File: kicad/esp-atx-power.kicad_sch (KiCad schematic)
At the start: 55 parts, among them J101 Conn_ARM_JTAG_SWD_10, J102 Conn_02x09_Odd_Even, J103 Conn_01x04, J105 GT-USB-7010ASV, K101 G3VM-61D1, K102 G3VM-61D1, K103 G3VM-61D1, K104 G3VM-61D1, SW101 TS-1187A-B-A-B, SW102 TS-1187A-B-A-B, U101 ESP32-C3-WROOM-02U, U102 AMS1117-3.3, U103 USBLC6-2P6, U104 TPS2116DRL

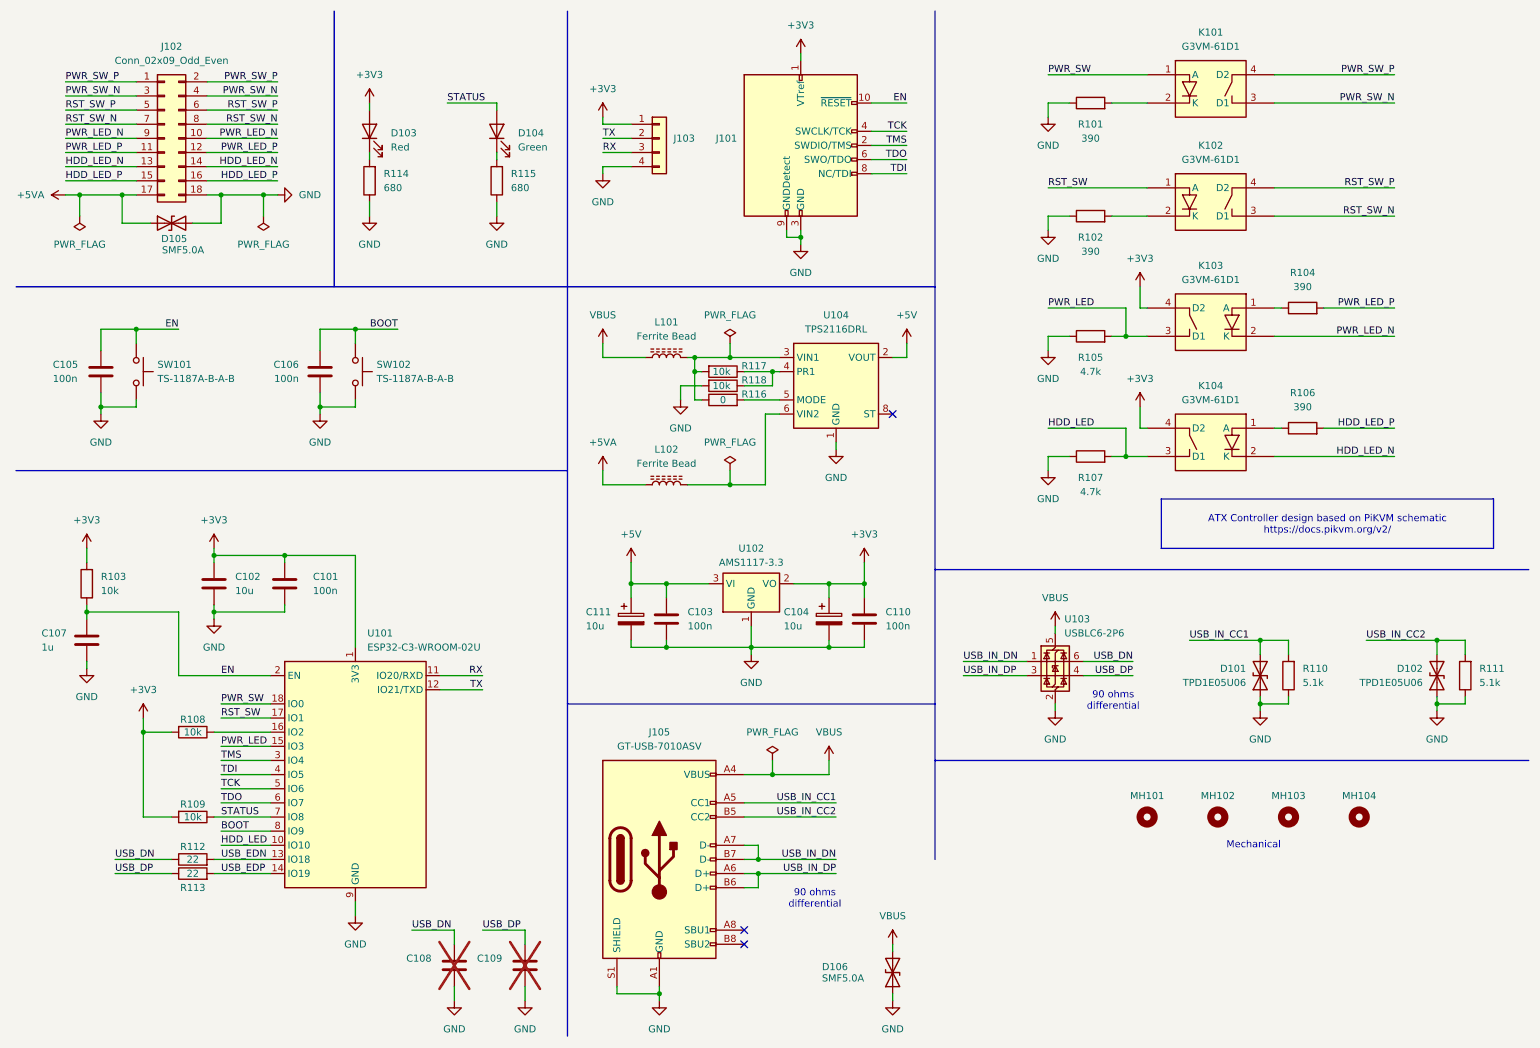
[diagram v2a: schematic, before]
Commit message: Fix TVS diode orientation
The selected diode was not bidirectional, update schematic symbol
to take it into account and fix orientation on VBUS (short circuit).
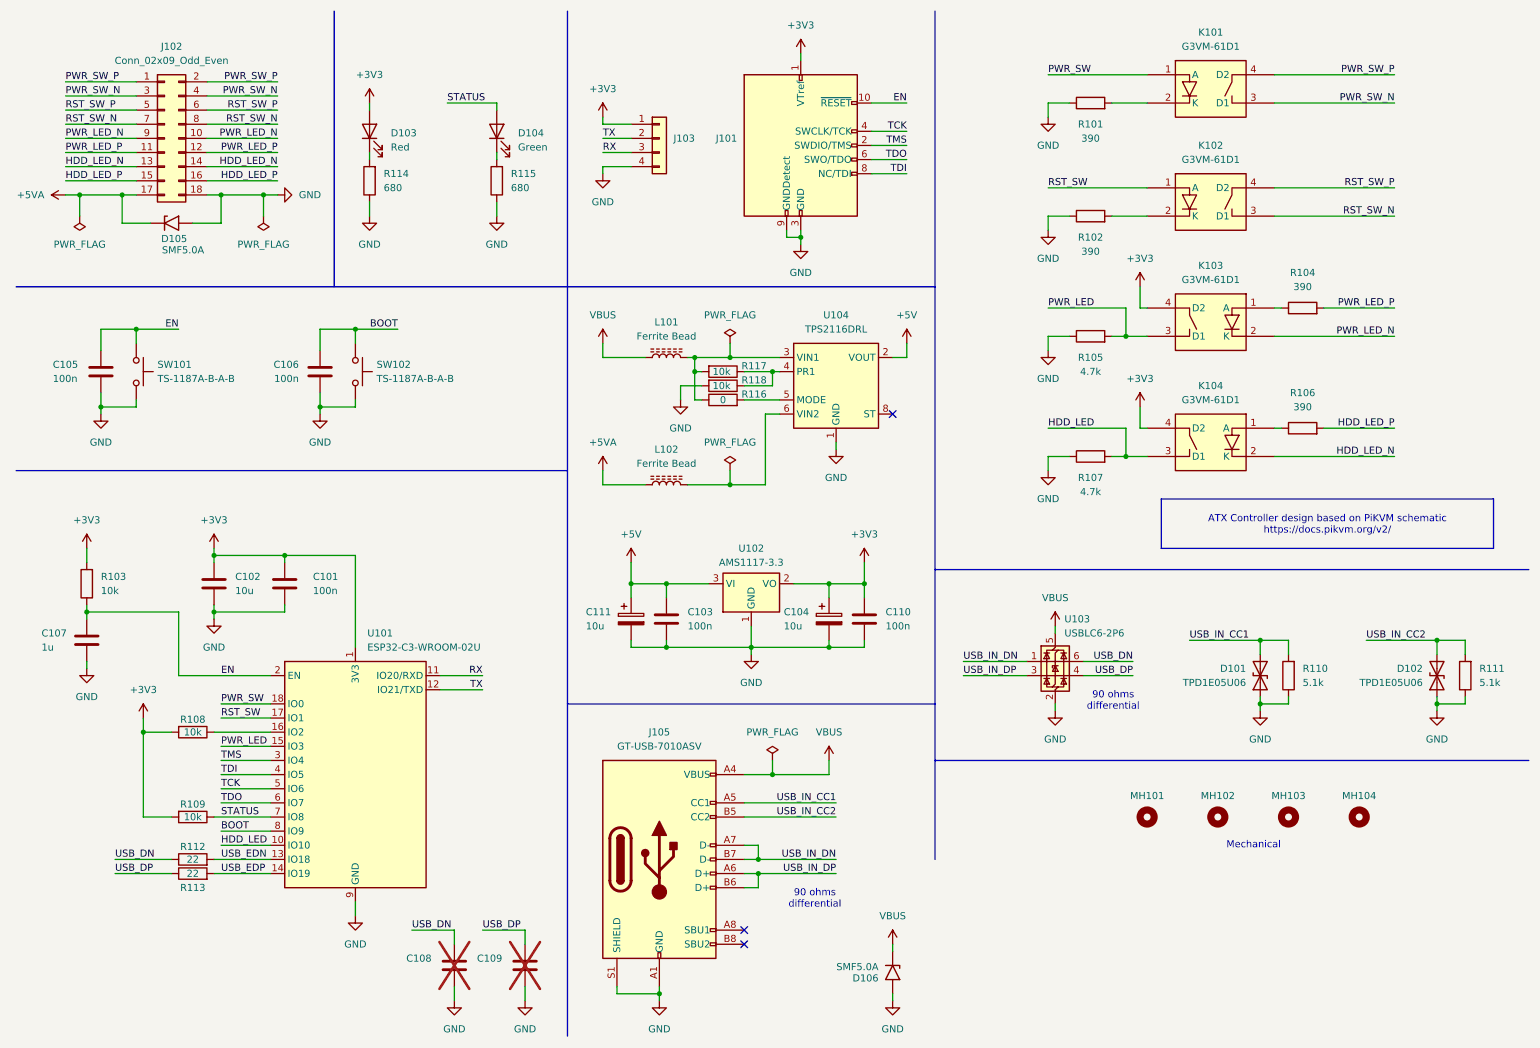
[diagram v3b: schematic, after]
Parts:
- D105, D106: symbol Device:D_TVS -> Diode:SMF5V0A
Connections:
- net GND: now also D106.2 (A2); no longer D106.1 (A1)
- net VBUS: now also D106.1 (A1); no longer D106.2 (A2)
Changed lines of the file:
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@@
 	(title_block
 		(title "ESP32 ATX Power Controller")
-		(date "2025-09-08")
-		(rev "2.0.0")
+		(date "2025-09-25")
+		(rev "2.0.1")
 	)
 	(text "90 ohms\ndifferential"
@@
 	)
 	(symbol
-		(lib_id "Device:D_TVS")
+		(lib_id "Diode:SMF5V0A")
 		(at 40.64 50.8 0)
 		(unit 1)
@@
 	)
 	(symbol
-		(lib_id "Device:D_TVS")
-		(at 170.18 185.42 90)
+		(lib_id "Diode:SMF5V0A")
+		(at 170.18 185.42 270)
 		(unit 1)
 		(exclude_from_sim no)
@@
 		(dnp no)
 		(property "Reference" "D106"
-			(at 157.48 184.404 90)
+			(at 167.64 186.436 90)
 			(effects
 				(font
@@
 		)
 		(property "Value" "SMF5.0A"
-			(at 157.48 186.436 90)
+			(at 167.64 184.404 90)
 			(effects
 				(font

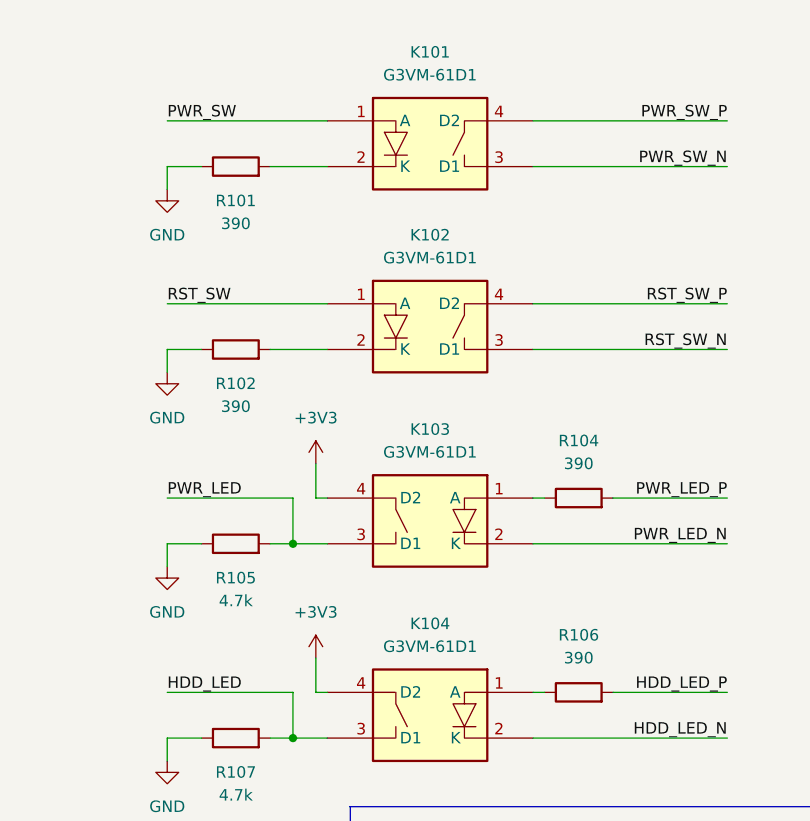
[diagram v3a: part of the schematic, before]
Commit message: Update obsolete components
- G3VM-61D1 is obselete and not manufactured anymore. A similar
reference has been set with smaller package
- Molex connector for debug is not available on JLCPCB anymore.
Alternative found with similar footprint
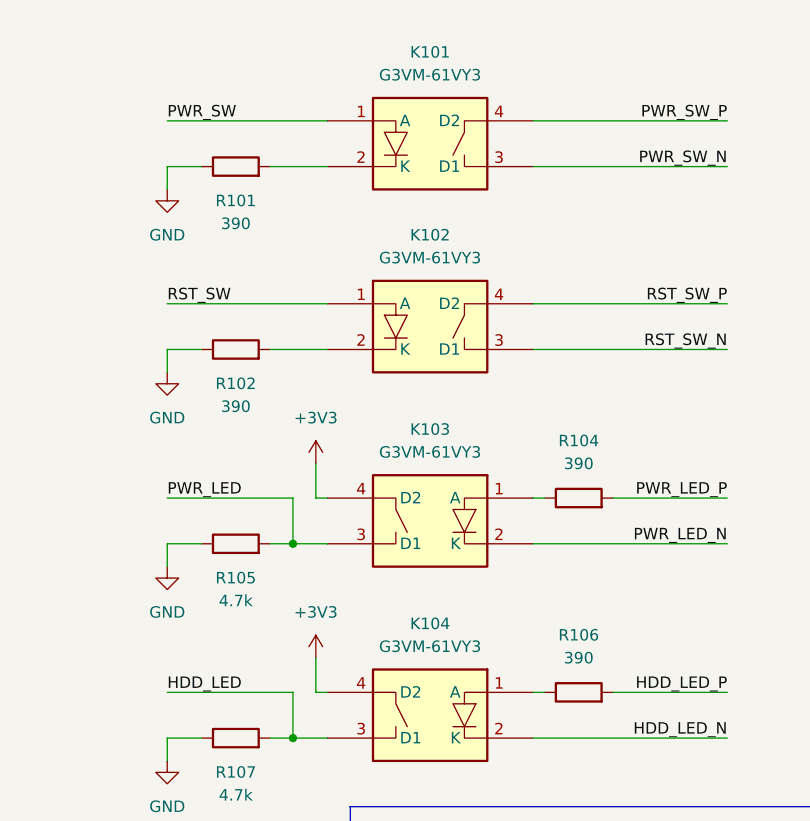
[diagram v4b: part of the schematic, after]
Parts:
- removed K101, K102, K103, K104: G3VM-61D1, Package_DIP:DIP-4_W8.89mm_SMDSocket_LongPads, symbol G3VM-61D1:G3VM-61D1
- added K101, K102, K103, K104: G3VM-61VY3, Package_SO:SOP-4_3.8x4.1mm_P2.54mm, symbol G3VM-61VY3:G3VM-61VY3
- J103: LCSC Part # C240847 -> C31597; MFR Part # 532610471 -> 1.25T-4PSurface Mount，Right Angle; Manufacturer MOLEX -> BOOMELE(Boom Precision Elec)
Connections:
- net +3V3: now also K103.4 (D2), K104.4 (D2)
- net HDD_LED: now also K104.3 (D1)
- net HDD_LED_N: now also K104.2 (K)
- net PWR_LED: now also K103.3 (D1)
- net PWR_LED_N: now also K103.2 (K)
- net PWR_SW: now also K101.1 (A)
- net PWR_SW_N: now also K101.3 (D1)
- net PWR_SW_P: now also K101.4 (D2)
- net RST_SW: now also K102.1 (A)
- net RST_SW_N: now also K102.3 (D1)
- net RST_SW_P: now also K102.4 (D2)
- net at R104.1: now also K103.1 (A)
- net at R101.2: now also K101.2 (K)
- net at R102.2: now also K102.2 (K)
- net at R106.1: now also K104.1 (A)
